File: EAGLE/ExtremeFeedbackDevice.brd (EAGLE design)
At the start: 57 x 66 mm, 23 parts, among them CON1 FTDI, CON2 SIGNAL, IC1 ESP-WROOM-02, IC2 IC2, SW1 RSTSW, SW2 PROGSW

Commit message: Finished first pcb work.
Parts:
- moved R7 3.04 mm to (28.4, 30.0)
- moved R1 2.00 mm to (31.2, 19.1)
- moved R10 2.00 mm to (27.4, 19.1)
- moved R8 2.00 mm to (20.0, 19.1)
- moved R9 2.00 mm to (23.6, 19.1)
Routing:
- net N$2: track 114.4 -> 102.6 mm
- net N$16: track 48.8 -> 58.0 mm, vias 1 -> 2
- net N$8: track 105.5 -> 113.8 mm
- net N$9: track 118.7 -> 111.1 mm
- net N$15: track 25.3 -> 30.9 mm
- net +3V3: track 111.8 -> 108.9 mm
- net GND: track 189.3 -> 187.6 mm
- net N$6: track 13.2 -> 12.1 mm
- net N$5: track 16.3 -> 17.2 mm
- net N$11: track 9.45 -> 8.63 mm
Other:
- board text added: "Extreme Feedback Device"
- board text added: "https://github.com/kekyo/ExtremeFeedbackDevice"

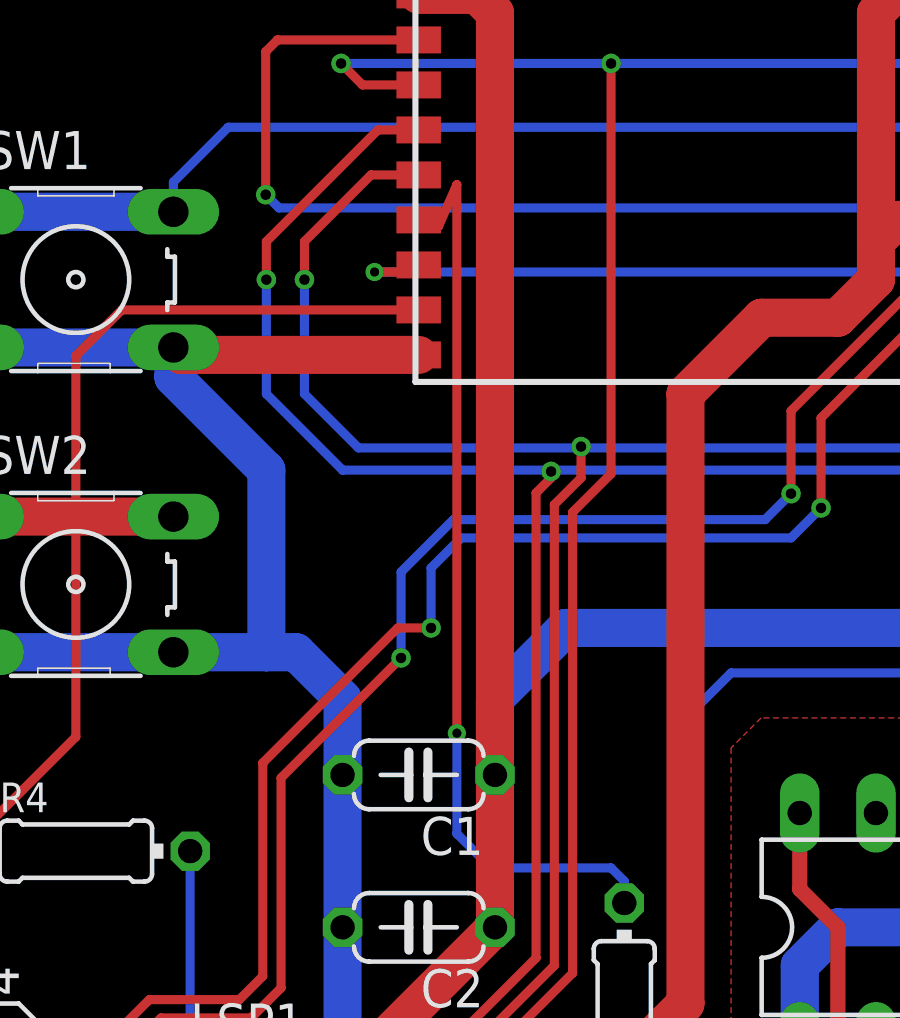
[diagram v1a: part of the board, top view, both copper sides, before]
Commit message: Fixed shifted line (Invalid in DRC)
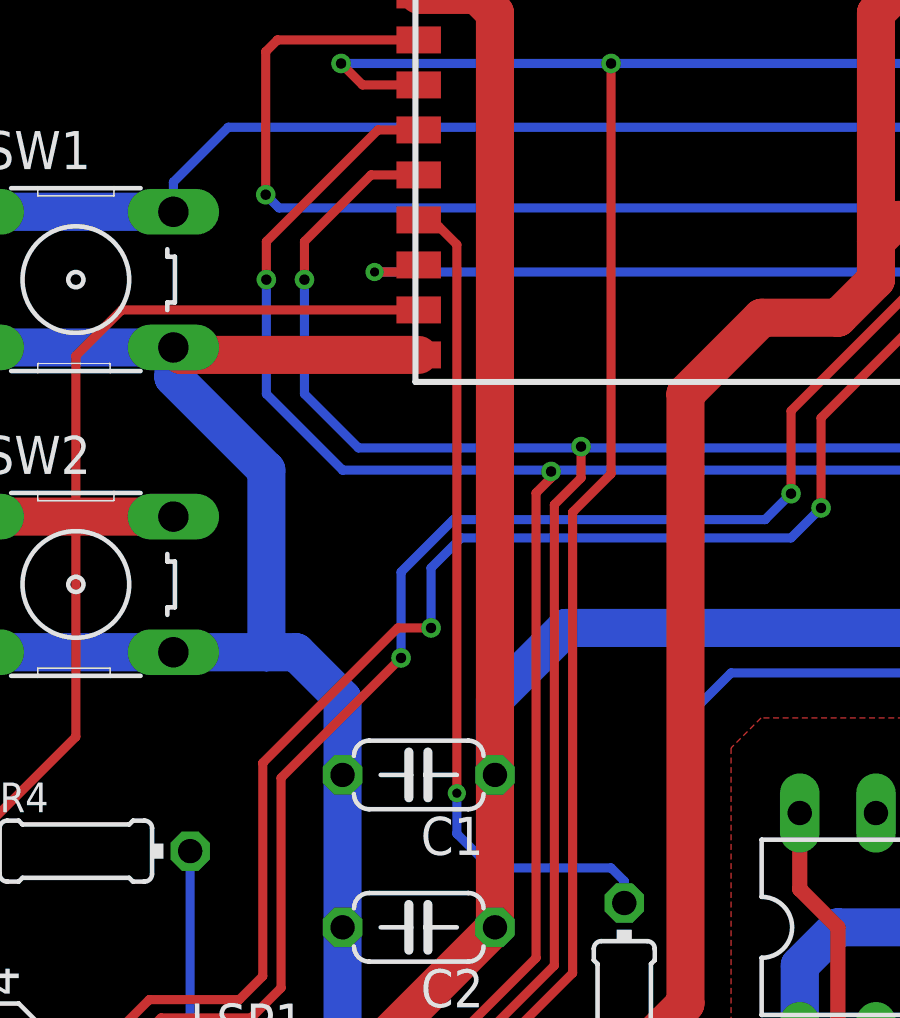
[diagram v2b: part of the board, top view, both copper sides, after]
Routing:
- net N$15: track 30.9 -> 28.3 mm
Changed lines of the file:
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@@
 <contactref element="R7" pad="2"/>
 <wire x1="22.2504" y1="56.388" x2="21.6408" y2="56.388" width="0.3048" layer="1"/>
-<wire x1="22.86" y1="57.7784" x2="22.2504" y2="56.388" width="0.3048" layer="1"/>
-<wire x1="22.86" y1="39.4904" x2="22.86" y2="57.7784" width="0.3048" layer="1"/>
+<wire x1="22.86" y1="55.7784" x2="22.2504" y2="56.388" width="0.3048" layer="1"/>
+<wire x1="22.86" y1="37.4904" x2="22.86" y2="55.7784" width="0.3048" layer="1"/>
 <wire x1="21.6408" y1="56.388" x2="21.5875" y2="56.6" width="0.3048" layer="1"/>
-<via x="22.86" y="39.4904" extent="1-16" drill="0.3048"/>
-<wire x1="22.86" y1="39.4904" x2="22.86" y2="36.14" width="0.3048" layer="16"/>
+<via x="22.86" y="37.4904" extent="1-16" drill="0.3048"/>
+<wire x1="22.86" y1="37.4904" x2="22.86" y2="36.14" width="0.3048" layer="16"/>
 <wire x1="22.86" y1="36.14" x2="24" y2="35" width="0.3048" layer="16"/>
 <wire x1="28" y1="35" x2="28.44" y2="34.56" width="0.3048" layer="16"/>
